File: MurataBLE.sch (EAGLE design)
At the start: 39 parts, among them CON1 C-2235, IC1 I-5448, IC3 74LVC1G00DBV, Q1 FC-135 32.7680KA-AG3, Q2 12MHz, SW1 P8073, SW2 P8073, SW3 P8073, U1 IC_BLE_LBCA2HNZYZ-711, X1 TSW-112-02-S-S

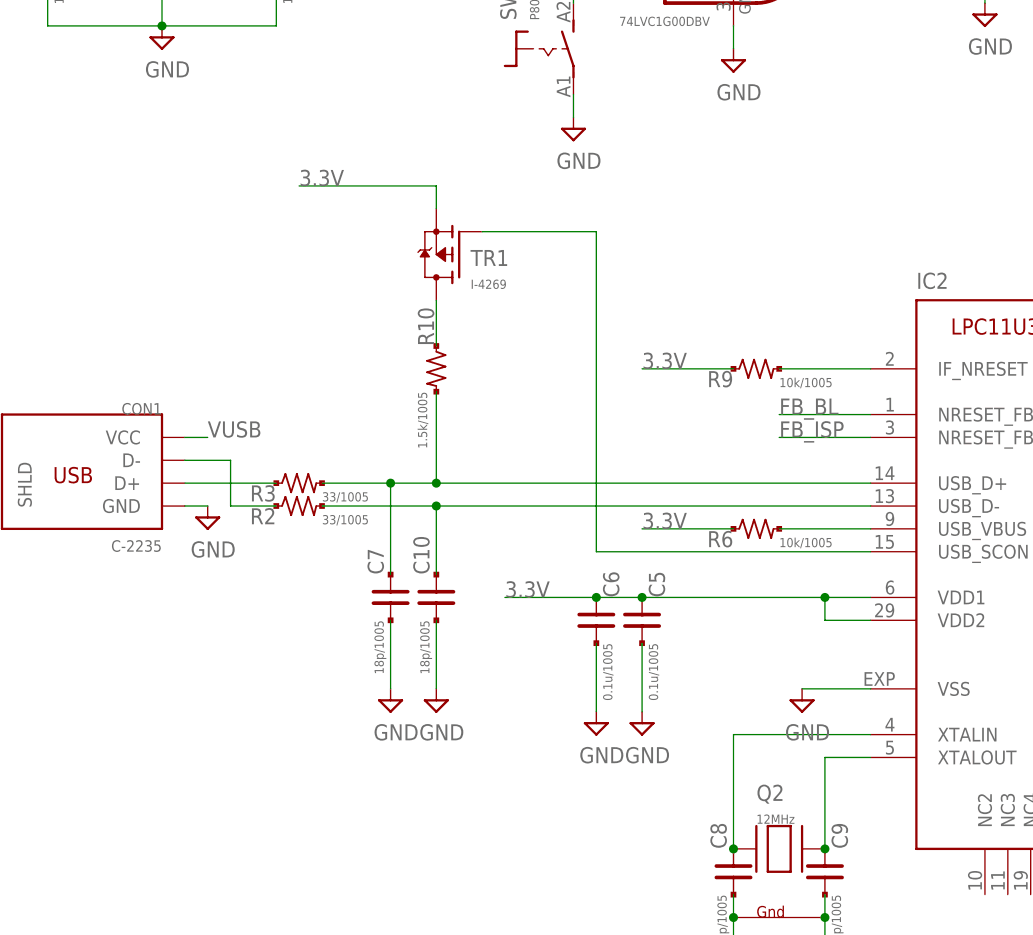
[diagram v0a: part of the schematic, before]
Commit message: [ USB ][ FIX ] USB connection
Fix USB line connection over R2,3,10, C7,10 and TR1
referenced to AN11392,NXP
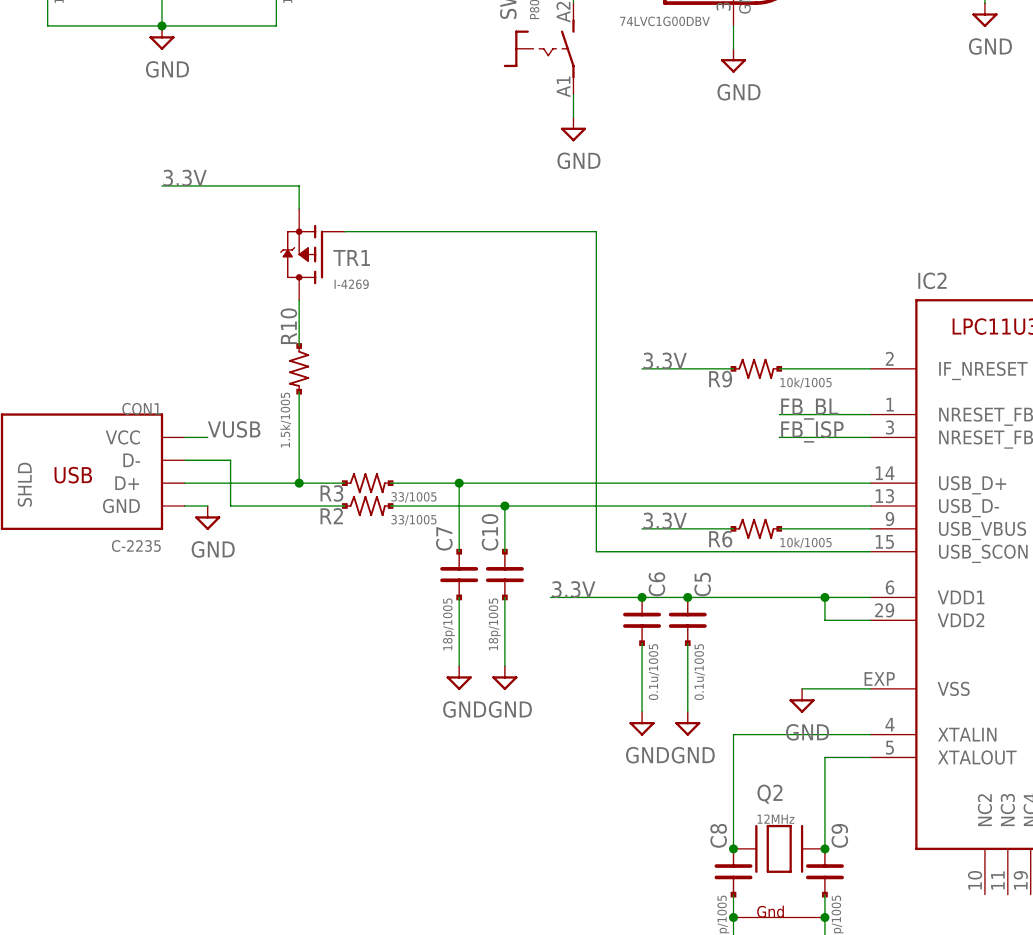
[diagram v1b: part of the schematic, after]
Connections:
- net N$20: no longer R10.2
- net N$21: now also R10.2
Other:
- moved on the sheet: C10, C5, C6, C7, R10, R2, R3, TR1
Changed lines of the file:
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@@
 <instance part="SUPPLY5" gate="GND" x="38.1" y="88.9"/>
 <instance part="SUPPLY6" gate="GND" x="33.02" y="142.24"/>
-<instance part="R2" gate="G$1" x="48.26" y="91.44"/>
-<instance part="R3" gate="G$1" x="48.26" y="93.98"/>
+<instance part="R2" gate="G$1" x="55.88" y="91.44"/>
+<instance part="R3" gate="G$1" x="55.88" y="93.98"/>
 <instance part="SUPPLY7" gate="GND" x="96.52" y="139.7"/>
 <instance part="SW2" gate="G$1" x="160.02" y="139.7"/>
@@
 <instance part="SUPPLY10" gate="GND" x="124.46" y="144.78"/>
 <instance part="SUPPLY2" gate="GND" x="78.74" y="132.08"/>
-<instance part="C5" gate="G$1" x="86.36" y="78.74"/>
-<instance part="C6" gate="G$1" x="81.28" y="78.74"/>
-<instance part="SUPPLY11" gate="GND" x="86.36" y="66.04"/>
-<instance part="SUPPLY12" gate="GND" x="81.28" y="66.04"/>
+<instance part="C5" gate="G$1" x="91.44" y="78.74"/>
+<instance part="C6" gate="G$1" x="86.36" y="78.74"/>
+<instance part="SUPPLY11" gate="GND" x="91.44" y="66.04"/>
+<instance part="SUPPLY12" gate="GND" x="86.36" y="66.04"/>
 <instance part="SUPPLY13" gate="GND" x="248.92" y="63.5"/>
 <instance part="X1" gate="-1" x="228.6" y="91.44" rot="MR0"/>
@@
 <instance part="X1" gate="-11" x="228.6" y="66.04" rot="MR0"/>
 <instance part="X1" gate="-12" x="228.6" y="63.5" rot="MR0"/>
-<instance part="C7" gate="G$1" x="58.42" y="81.28" rot="MR0"/>
-<instance part="C10" gate="G$1" x="63.5" y="81.28" rot="MR0"/>
-<instance part="SUPPLY14" gate="GND" x="63.5" y="68.58"/>
-<instance part="SUPPLY15" gate="GND" x="58.42" y="68.58"/>
-<instance part="TR1" gate="G$1" x="63.5" y="119.38" rot="MR0"/>
-<instance part="R10" gate="G$1" x="63.5" y="106.68" rot="R270"/>
+<instance part="C7" gate="G$1" x="66.04" y="83.82" rot="MR0"/>
+<instance part="C10" gate="G$1" x="71.12" y="83.82" rot="MR0"/>
+<instance part="SUPPLY14" gate="GND" x="71.12" y="71.12"/>
+<instance part="SUPPLY15" gate="GND" x="66.04" y="71.12"/>
+<instance part="TR1" gate="G$1" x="48.26" y="119.38" rot="MR0"/>
+<instance part="R10" gate="G$1" x="48.26" y="106.68" rot="R270"/>
 <instance part="IC3" gate="A" x="96.52" y="152.4" smashed="yes">
 <attribute name="NAME" x="88.9" y="158.115" size="1.778" layer="95"/>
@@
 <pinref part="C5" gate="G$1" pin="2"/>
 <pinref part="SUPPLY11" gate="GND" pin="GND"/>
-<wire x1="86.36" y1="76.2" x2="86.36" y2="68.58" width="0.1524" layer="91"/>
+<wire x1="91.44" y1="76.2" x2="91.44" y2="68.58" width="0.1524" layer="91"/>
 </segment>
 <segment>
 <pinref part="C6" gate="G$1" pin="2"/>
 <pinref part="SUPPLY12" gate="GND" pin="GND"/>
-<wire x1="81.28" y1="76.2" x2="81.28" y2="68.58" width="0.1524" layer="91"/>
+<wire x1="86.36" y1="76.2" x2="86.36" y2="68.58" width="0.1524" layer="91"/>
 </segment>
 <segment>
@@
 <pinref part="C10" gate="G$1" pin="2"/>
 <pinref part="SUPPLY14" gate="GND" pin="GND"/>
-<wire x1="63.5" y1="71.12" x2="63.5" y2="78.74" width="0.1524" layer="91"/>
+<wire x1="71.12" y1="73.66" x2="71.12" y2="81.28" width="0.1524" layer="91"/>
 </segment>
 <segment>
 <pinref part="C7" gate="G$1" pin="2"/>
 <pinref part="SUPPLY15" gate="GND" pin="GND"/>
-<wire x1="58.42" y1="71.12" x2="58.42" y2="78.74" width="0.1524" layer="91"/>
+<wire x1="66.04" y1="73.66" x2="66.04" y2="81.28" width="0.1524" layer="91"/>
 </segment>
 <segment>
@@
 </segment>
 <segment>
-<wire x1="106.68" y1="81.28" x2="86.36" y2="81.28" width="0.1524" layer="91"/>
+<wire x1="106.68" y1="81.28" x2="91.44" y2="81.28" width="0.1524" layer="91"/>
 <pinref part="IC2" gate="G$1" pin="VDD1"/>
-<wire x1="86.36" y1="81.28" x2="81.28" y2="81.28" width="0.1524" layer="91"/>
-<wire x1="81.28" y1="81.28" x2="71.12" y2="81.28" width="0.1524" layer="91"/>
+<wire x1="91.44" y1="81.28" x2="86.36" y2="81.28" width="0.1524" layer="91"/>
+<wire x1="86.36" y1="81.28" x2="76.2" y2="81.28" width="0.1524" layer="91"/>
 <wire x1="111.76" y1="81.28" x2="106.68" y2="81.28" width="0.1524" layer="91"/>
 <wire x1="106.68" y1="81.28" x2="106.68" y2="78.74" width="0.1524" layer="91"/>
@@
 <wire x1="106.68" y1="78.74" x2="111.76" y2="78.74" width="0.1524" layer="91"/>
 <junction x="106.68" y="81.28"/>
-<label x="71.12" y="81.28" size="1.778" layer="95"/>
+<label x="76.2" y="81.28" size="1.778" layer="95"/>
 <pinref part="C6" gate="G$1" pin="1"/>
-<junction x="81.28" y="81.28"/>
+<junction x="86.36" y="81.28"/>
 <pinref part="C5" gate="G$1" pin="1"/>
-<junction x="86.36" y="81.28"/>
+<junction x="91.44" y="81.28"/>
 </segment>
 <segment>
@@
 </segment>
 <segment>
-<wire x1="63.5" y1="124.46" x2="63.5" y2="127" width="0.1524" layer="91"/>
-<wire x1="63.5" y1="127" x2="48.26" y2="127" width="0.1524" layer="91"/>
+<wire x1="48.26" y1="124.46" x2="48.26" y2="127" width="0.1524" layer="91"/>
+<wire x1="48.26" y1="127" x2="33.02" y2="127" width="0.1524" layer="91"/>
 <pinref part="TR1" gate="G$1" pin="S"/>
-<label x="48.26" y="127" size="1.778" layer="95"/>
+<label x="33.02" y="127" size="1.778" layer="95"/>
 </segment>
 </net>
@@
 <segment>
 <pinref part="CON1" gate="G$1" pin="D+"/>
-<wire x1="35.56" y1="93.98" x2="45.72" y2="93.98" width="0.1524" layer="91"/>
+<wire x1="35.56" y1="93.98" x2="48.26" y2="93.98" width="0.1524" layer="91"/>
 <pinref part="R3" gate="G$1" pin="1"/>
+<pinref part="R10" gate="G$1" pin="2"/>
+<wire x1="48.26" y1="93.98" x2="53.34" y2="93.98" width="0.1524" layer="91"/>
+<wire x1="48.26" y1="104.14" x2="48.26" y2="93.98" width="0.1524" layer="91"/>
+<junction x="48.26" y="93.98"/>
 </segment>
 </net>
@@
 <wire x1="35.56" y1="96.52" x2="40.64" y2="96.52" width="0.1524" layer="91"/>
 <wire x1="40.64" y1="96.52" x2="40.64" y2="91.44" width="0.1524" layer="91"/>
-<wire x1="40.64" y1="91.44" x2="45.72" y2="91.44" width="0.1524" layer="91"/>
+<wire x1="40.64" y1="91.44" x2="53.34" y2="91.44" width="0.1524" layer="91"/>
 <pinref part="R2" gate="G$1" pin="1"/>
 </segment>
@@
 <pinref part="IC2" gate="G$1" pin="USB_D+"/>
 <pinref part="R3" gate="G$1" pin="2"/>
-<wire x1="50.8" y1="93.98" x2="58.42" y2="93.98" width="0.1524" layer="91"/>
+<wire x1="58.42" y1="93.98" x2="66.04" y2="93.98" width="0.1524" layer="91"/>
 <pinref part="C7" gate="G$1" pin="1"/>
-<wire x1="58.42" y1="93.98" x2="63.5" y2="93.98" width="0.1524" layer="91"/>
-<wire x1="63.5" y1="93.98" x2="111.76" y2="93.98" width="0.1524" layer="91"/>
-<wire x1="58.42" y1="83.82" x2="58.42" y2="93.98" width="0.1524" layer="91"/>
-<junction x="58.42" y="93.98"/>
-<pinref part="R10" gate="G$1" pin="2"/>
-<wire x1="63.5" y1="104.14" x2="63.5" y2="93.98" width="0.1524" layer="91"/>
-<junction x="63.5" y="93.98"/>
+<wire x1="66.04" y1="93.98" x2="111.76" y2="93.98" width="0.1524" layer="91"/>
+<wire x1="66.04" y1="86.36" x2="66.04" y2="93.98" width="0.1524" layer="91"/>
+<junction x="66.04" y="93.98"/>
 </segment>
 </net>
@@
 <pinref part="IC2" gate="G$1" pin="USB_D-"/>
 <pinref part="R2" gate="G$1" pin="2"/>
-<wire x1="50.8" y1="91.44" x2="63.5" y2="91.44" width="0.1524" layer="91"/>
+<wire x1="58.42" y1="91.44" x2="71.12" y2="91.44" width="0.1524" layer="91"/>
 <pinref part="C10" gate="G$1" pin="1"/>
-<wire x1="63.5" y1="91.44" x2="111.76" y2="91.44" width="0.1524" layer="91"/>
-<wire x1="63.5" y1="83.82" x2="63.5" y2="91.44" width="0.1524" layer="91"/>
-<junction x="63.5" y="91.44"/>
+<wire x1="71.12" y1="91.44" x2="111.76" y2="91.44" width="0.1524" layer="91"/>
+<wire x1="71.12" y1="86.36" x2="71.12" y2="91.44" width="0.1524" layer="91"/>
+<junction x="71.12" y="91.44"/>
 </segment>
 </net>
@@
 <pinref part="TR1" gate="G$1" pin="D"/>
 <pinref part="R10" gate="G$1" pin="1"/>
-<wire x1="63.5" y1="114.3" x2="63.5" y2="109.22" width="0.1524" layer="91"/>
+<wire x1="48.26" y1="114.3" x2="48.26" y2="109.22" width="0.1524" layer="91"/>
 </segment>
 </net>
@@
 <wire x1="81.28" y1="86.36" x2="81.28" y2="121.92" width="0.1524" layer="91"/>
 <pinref part="TR1" gate="G$1" pin="G"/>
-<wire x1="81.28" y1="121.92" x2="68.58" y2="121.92" width="0.1524" layer="91"/>
-</segment>
-</net>
+<wire x1="81.28" y1="121.92" x2="53.34" y2="121.92" width="0.1524" layer="91"/>
+</segment>
+</net>

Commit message: [ USB ] lisence stated
CC-BY-SA
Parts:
- added TP5, TP6, TP7, TP8: TPTP06R, testpad_local:TPTP06R
- TP1, TP2, TP3, TP4: value TPTP07SQ -> TPTP06SQ; device testpad_local:TPTP07SQ -> testpad_local:TPTP06SQ
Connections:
- net P0_0: now also TP8.TP
- net P0_1: now also TP7.TP
- net TGT_RX: now also TP6.TP
- net TGT_TX: now also TP5.TP
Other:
- note added: "-> <-"
- note added: "<- ->"
- note added: "CC-BY-SA"
- moved on the sheet: TP2, TP4
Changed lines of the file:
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@@
 <part name="R10" library="mylib" deviceset="R_US_PAD_PAD" device="_1005" value="1.5k/1005"/>
 <part name="IC3" library="74xx-little-us_local" deviceset="74*1G00" device="DBV" technology="LVC" value="74LVC1G00DBV"/>
-<part name="TP1" library="testpad_local" deviceset="TP" device="TP07SQ"/>
-<part name="TP2" library="testpad_local" deviceset="TP" device="TP07SQ"/>
-<part name="TP3" library="testpad_local" deviceset="TP" device="TP07SQ"/>
-<part name="TP4" library="testpad_local" deviceset="TP" device="TP07SQ"/>
+<part name="TP1" library="testpad_local" deviceset="TP" device="TP06SQ" value="TPTP06SQ"/>
+<part name="TP2" library="testpad_local" deviceset="TP" device="TP06SQ" value="TPTP06SQ"/>
+<part name="TP3" library="testpad_local" deviceset="TP" device="TP06SQ" value="TPTP06SQ"/>
+<part name="TP4" library="testpad_local" deviceset="TP" device="TP06SQ" value="TPTP06SQ"/>
 <part name="R4" library="mylib" deviceset="R_US_PAD_PAD" device="_1005" value="270/1005"/>
 <part name="R5" library="mylib" deviceset="R_US_PAD_PAD" device="_1005" value="75/1005"/>
@@
 <part name="SUPPLY16" library="mylib" deviceset="GND" device=""/>
 <part name="LED1" library="mylib" deviceset="LED_3SEG" device=""/>
+<part name="TP5" library="testpad_local" deviceset="TP" device="TP06R" value="TPTP06R"/>
+<part name="TP6" library="testpad_local" deviceset="TP" device="TP06R" value="TPTP06R"/>
+<part name="TP7" library="testpad_local" deviceset="TP" device="TP06R" value="TPTP06R"/>
+<part name="TP8" library="testpad_local" deviceset="TP" device="TP06R" value="TPTP06R"/>
 </parts>
 <sheets>
@@
 (G) = 2.9V
 (B) = 2.8V</text>
+<text x="187.96" y="68.58" size="1.778" layer="94">&lt;-
+-&gt;</text>
+<text x="241.3" y="139.7" size="1.778" layer="94">-&gt;
+&lt;-</text>
+<text x="226.06" y="20.32" size="2.54" layer="94">CC-BY-SA</text>
 </plain>
 <instances>
@@
 <instance part="IC3" gate="P" x="96.52" y="152.4"/>
 <instance part="TP1" gate="G$1" x="175.26" y="71.12" rot="R270"/>
-<instance part="TP2" gate="G$1" x="180.34" y="71.12" rot="R90"/>
+<instance part="TP2" gate="G$1" x="182.88" y="71.12" rot="R90"/>
 <instance part="TP3" gate="G$1" x="175.26" y="68.58" rot="R270"/>
-<instance part="TP4" gate="G$1" x="180.34" y="68.58" rot="R90"/>
+<instance part="TP4" gate="G$1" x="182.88" y="68.58" rot="R90"/>
 <instance part="R4" gate="G$1" x="165.1" y="106.68"/>
 <instance part="R5" gate="G$1" x="165.1" y="104.14"/>
@@
 <instance part="LED1" gate="G" x="175.26" y="104.14" rot="R90"/>
 <instance part="LED1" gate="B" x="177.8" y="101.6" rot="R90"/>
+<instance part="TP5" gate="G$1" x="172.72" y="73.66"/>
+<instance part="TP6" gate="G$1" x="172.72" y="66.04" rot="R180"/>
+<instance part="TP7" gate="G$1" x="185.42" y="66.04" rot="R180"/>
+<instance part="TP8" gate="G$1" x="185.42" y="73.66"/>
 </instances>
 <busses>
@@
 </segment>
 <segment>
-<wire x1="190.5" y1="71.12" x2="182.88" y2="71.12" width="0.1524" layer="91"/>
-<label x="190.5" y="71.12" size="1.778" layer="95"/>
+<wire x1="193.04" y1="71.12" x2="185.42" y2="71.12" width="0.1524" layer="91"/>
+<label x="193.04" y="71.12" size="1.778" layer="95"/>
 <pinref part="TP2" gate="G$1" pin="TP"/>
+<pinref part="TP8" gate="G$1" pin="TP"/>
+<junction x="185.42" y="71.12"/>
 </segment>
 </net>
@@
 </segment>
 <segment>
-<wire x1="190.5" y1="68.58" x2="182.88" y2="68.58" width="0.1524" layer="91"/>
-<label x="190.5" y="68.58" size="1.778" layer="95"/>
+<wire x1="193.04" y1="68.58" x2="185.42" y2="68.58" width="0.1524" layer="91"/>
+<label x="193.04" y="68.58" size="1.778" layer="95"/>
 <pinref part="TP4" gate="G$1" pin="TP"/>
+<pinref part="TP7" gate="G$1" pin="TP"/>
+<junction x="185.42" y="68.58"/>
 </segment>
 </net>
@@
 <pinref part="TP1" gate="G$1" pin="TP"/>
 <wire x1="172.72" y1="71.12" x2="157.48" y2="71.12" width="0.1524" layer="91"/>
+<pinref part="TP5" gate="G$1" pin="TP"/>
+<junction x="172.72" y="71.12"/>
 </segment>
 </net>
@@
 <pinref part="TP3" gate="G$1" pin="TP"/>
 <wire x1="172.72" y1="68.58" x2="157.48" y2="68.58" width="0.1524" layer="91"/>
-</segment>
-</net>
+<pinref part="TP6" gate="G$1" pin="TP"/>
+<junction x="172.72" y="68.58"/>
+</segment>
+</net>
